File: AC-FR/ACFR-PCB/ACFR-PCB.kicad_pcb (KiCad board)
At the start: 4 copper layers, 46 x 26 mm, 65 parts, among them J1 USB4105-GF-A, J2 Micro_SD_Card_Det1, J3 JST-SM04B-SRSS, J4 JST-PH, Q1 DMP2045U-7, Q2 DMP2045U-7, SW1 PTS636 SK25F, SW2 PTS636 SK25F, U1 ESP32-S3R8, U2 BMP390, U3 W25Q128JVPIQ, U4 W25Q128JVPIQ, U5 LSM6DSO32, U6 H3LIS331DLTR, U7 AP2112K-3.3TRG1, U8 LIS3MDL, U9 AP2112K-3.3TRG1, Y1 ECS-400-8-36B-7KY

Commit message: Redo power
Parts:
- removed the C17 at (199.3, 115.3)
- removed C19, C21: 10uF, Capacitor_SMD:C_0603_1608Metric
- removed the C7 at (41.1, 155.3)
- removed H3: M2.5_2.7mm, MountingHole:MountingHole_2.7mm_M2.5_Pad_Via
- removed TP3: TestPoint, TestPoint:TestPoint_Pad_D1.5mm
- removed U9: AP2112K-3.3TRG1, Package_TO_SOT_SMD:SOT-23-5
- added C15: 1uF, Capacitor_SMD:C_0603_1608Metric, F.Cu at (162.6, 91.0)
- BZ1, D2, J2, J3, Q1, R10, R11, R12, R13, R4, R8, R9, U4: moved to B.Cu
- C11: renamed from C12; moved to B.Cu
- H1, H2: footprint MountingHole:MountingHole_2.7mm_M2.5_Pad_Via -> besser_footprints:M2.5_2.7mm_hole
- U7: value AP2112K-3.3TRG1 -> NCP187AMT330TAG; footprint Package_TO_SOT_SMD:SOT-23-5 -> besser_footprints:6-WDFN_2x2mm_EP
- moved J3 138.6 mm to (169.7, 98.3), turned to -90 degrees
- moved C6 125.4 mm to (164.4, 130.1)
- moved C7 119.4 mm to (134.7, 89.1), turned to 180 degrees
- moved U2 118.6 mm to (134.7, 91.1), turned to 90 degrees
- moved C5 117.2 mm to (157.8, 139.8), turned to -90 degrees
- moved C4 113.2 mm to (153.2, 132.2), turned to 180 degrees
- moved C3 113.0 mm to (153.2, 130.8), turned to 180 degrees
- moved R11 109.1 mm to (153.3, 102.3)
- moved R12 109.1 mm to (153.3, 105.3)
- moved R13 109.1 mm to (153.3, 108.3)
- moved C12 106.4 mm to (129.5, 97.2)
- moved U5 106.4 mm to (129.5, 94.8)
- moved C18 104.8 mm to (132.6, 94.8)
- moved U8 104.8 mm to (134.7, 94.8)
- moved C17 104.8 mm to (135.2, 97.0)
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- renumbered C11 to C10, C13 to C12, C14 to C13, C15 to C14, C18 to C17, C20 to C18, C8 to C7, C9 to C8, C10 to C9
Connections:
- C1 pad 1: +3V3_2 -> +3V3
- C11 pad 1: +3V3_2 -> +3V3
- C12 pad 1: +3V3_2 -> +3V3
- C13 pad 1: +3V3_2 -> +3V3
- C16 pad 2: VHIGH -> +3V3
- C17 pad 1: +3V3_2 -> +3V3
- C3 pad 1: +3V3_MCU -> +3V3
- C4 pad 1: +3V3_MCU -> +3V3
- C5 pad 1: +3V3_MCU -> +3V3
- C6 pad 1: +3V3_MCU -> +3V3
- C7 pad 2: +3V3_2 -> +3V3
- D1 pad 4: +3V3_2 -> +3V3
- J2 pad 11: GND -> (no net)
- J2 pad 12: GND -> (no net)
- J2 pad 4: +3V3_2 -> +3V3
- J2 pad 9: (no net) -> unconnected-(J2-DET-Pad9)
- R10 pad 1: +3V3_2 -> +3V3
- R11 pad 1: +3V3_2 -> +3V3
- R12 pad 1: +3V3_2 -> +3V3
- R13 pad 1: +3V3_2 -> +3V3
- R3 pad 2: +3V3_MCU -> +3V3
- R6 pad 2: +3V3_2 -> +3V3
- R7 pad 2: +3V3_2 -> +3V3
- R8 pad 1: +3V3_2 -> +3V3
- R9 pad 1: +3V3_2 -> +3V3
- TP1 pad 1: /IO11 -> /IO10
- TP2 pad 1: /IO12 -> /IO11
- U1 pad 10: /MISO -> /MOSI
- U1 pad 11: /SCK -> /MISO
- U1 pad 12: /FSH_CS -> /SCK
- U1 pad 14: /VBAT_SENSE -> /FSH_CS
- U1 pad 15: /NEOPIXEL -> /IO10
- U1 pad 17: /IO12 -> unconnected-(U1-GPIO12-Pad17)
- U1 pad 18: /IO13 -> unconnected-(U1-GPIO13-Pad18)
- U1 pad 19: /IMU_INT -> unconnected-(U1-GPIO14-Pad19)
- U1 pad 2: +3V3_MCU -> +3V3
- U1 pad 20: +3V3_MCU -> +3V3
- U1 pad 3: +3V3_MCU -> +3V3
- U1 pad 46: +3V3_MCU -> +3V3
- U1 pad 55: +3V3_MCU -> +3V3
- U1 pad 56: +3V3_MCU -> +3V3
- U1 pad 6: unconnected-(U1-GPIO1-Pad6) -> /NEOPIXEL
- U1 pad 9: /MOSI -> /VBAT_SENSE
- U2 pad 1: +3V3_2 -> +3V3
- U2 pad 10: +3V3_2 -> +3V3
- U2 pad 5: +3V3_2 -> +3V3
- U2 pad 6: +3V3_2 -> +3V3
- U4 pad 8: +3V3_2 -> +3V3
- U5 pad 12: +3V3_2 -> +3V3
- U5 pad 4: /IMU_INT -> unconnected-(U5-INT1-Pad4)
- U5 pad 5: +3V3_2 -> +3V3
- U5 pad 8: +3V3_2 -> +3V3
- U6 pad 1: +3V3_2 -> +3V3
- U6 pad 14: +3V3_2 -> +3V3
- U6 pad 15: +3V3_2 -> +3V3
- U6 pad 8: +3V3_2 -> +3V3
- U7 pad 2: GND -> VHIGH
- U7 pad 3: VHIGH -> GND
- U7 pad 5: +3V3_MCU -> +3V3
- U8 pad 10: +3V3_2 -> +3V3
- U8 pad 5: +3V3_2 -> +3V3
- U8 pad 6: +3V3_2 -> +3V3
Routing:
- net /SPICS0: track 0.00 -> 13.1 mm, vias 0 -> 2
- net /SPIQ: track 0.00 -> 11.2 mm, vias 0 -> 2
- net /SPIWP: track 0.00 -> 8.43 mm, vias 0 -> 2
- net /VDD_SPI: track 0.00 -> 6.91 mm
- net /SPIHD: track 0.00 -> 2.72 mm
- net /SPID: track 0.00 -> 2.61 mm
- net /SPICLK: track 0.00 -> 2.41 mm
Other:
- board text added: "3.7/4.2v 1S LiPo"

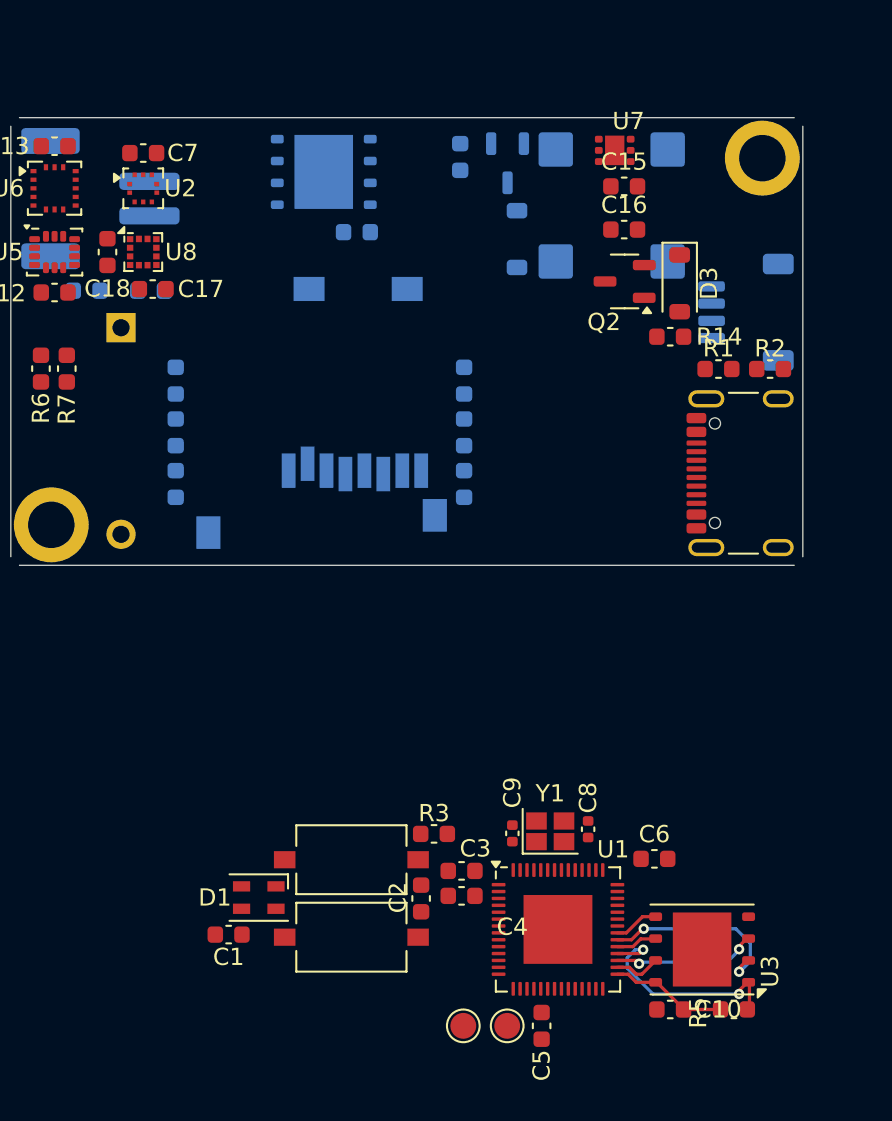
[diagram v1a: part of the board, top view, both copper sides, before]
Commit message: why do the colors not not stay after a crash this was supposed to be fixed in fucking 8.0.2
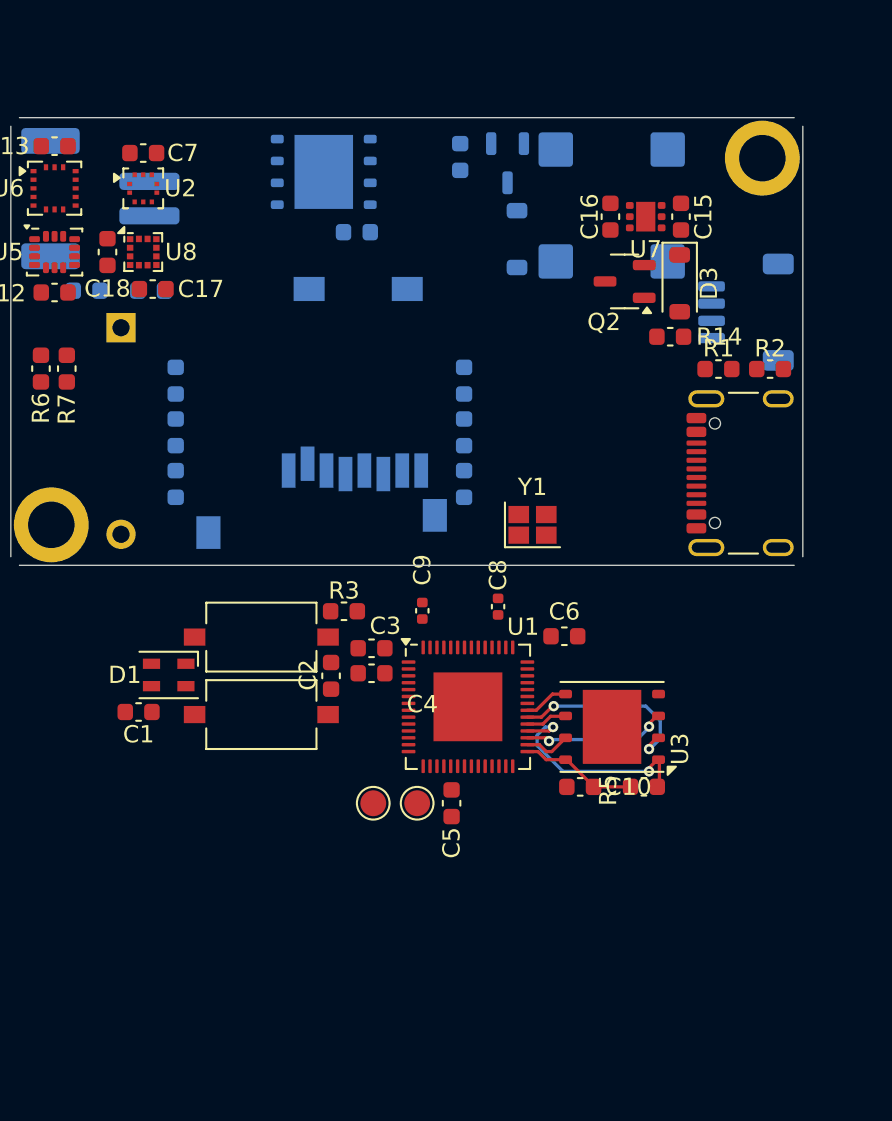
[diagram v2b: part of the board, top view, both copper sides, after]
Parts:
- moved Y1 17.8 mm to (157.3, 110.7)
- moved C10 13.9 mm to (160.1, 125.9)
- moved C3 13.9 mm to (147.9, 117.8)
- moved C5 13.9 mm to (152.6, 126.8)
- moved D1 13.9 mm to (136.2, 119.4)
- moved TP2 13.9 mm to (150.6, 126.8)
- moved C6 13.9 mm to (159.2, 117.1)
- moved C8 13.9 mm to (155.3, 115.4)
- moved TP1 13.9 mm to (148.1, 126.8)
- moved U1 13.9 mm to (153.6, 121.2)
- moved C1 13.9 mm to (134.4, 121.5)
- moved C2 13.9 mm to (145.6, 119.4)
- moved C4 13.9 mm to (147.9, 119.3)
- moved R3 13.9 mm to (146.3, 115.7)
- moved U3 13.9 mm to (161.9, 122.4)
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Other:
- board text added: "+"
- board text added: "-"
- board text added: "1S LiPo"
- board text added: "FD Flash"
- board text added: "R1 11-2024"
- board text removed: "3.7/4.2v 1S LiPo"

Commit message: Finalize part placement
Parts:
- C15, C16, D3, Q2, R14, U7: moved to B.Cu
- moved C15 38.0 mm to (128.6, 99.9)
- moved D3 37.5 mm to (129.0, 103.8)
- moved R14 36.7 mm to (129.3, 106.9), turned to 0 degrees
- moved C18 36.0 mm to (168.7, 94.2)
- moved C17 36.0 mm to (171.2, 96.2)
- moved C12 36.0 mm to (165.5, 96.5)
- moved U5 36.0 mm to (165.5, 94.2)
- moved U6 36.0 mm to (165.5, 90.5)
- moved U8 36.0 mm to (170.7, 94.2)
- moved C13 36.0 mm to (165.5, 88.2)
- moved U7 34.0 mm to (130.7, 99.9), turned to 0 degrees
- moved R6 32.8 mm to (160.7, 94.2)
- moved R7 32.8 mm to (162.2, 94.2)
- moved Q2 31.3 mm to (132.2, 103.7), turned to 0 degrees
- moved C16 30.0 mm to (132.7, 99.9)
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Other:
- outline, holes or cut-outs redrawn

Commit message: Start on routing (kill the project, its horrible)
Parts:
- removed J3: JST-SM04B-SRSS, besser_footprints:JST_SH_SM04B-SRSS-TB_1x04-1MP_P1.00mm_Horizontal
- added R8: 47k, Capacitor_SMD:C_0603_1608Metric, B.Cu at (161.3, 110.2)
- moved C3 30.8 mm to (146.8, 130.3)
- moved C5 30.8 mm to (151.7, 139.3)
- moved R3 30.8 mm to (146.8, 128.8)
- moved U3 30.8 mm to (160.8, 134.9)
- moved TP1 30.8 mm to (146.9, 139.3)
- moved TP2 30.8 mm to (149.5, 139.3)
- moved C4 30.8 mm to (146.8, 131.8)
- moved C6 30.8 mm to (155.8, 128.8)
- moved C9 30.8 mm to (148.8, 127.8)
- moved R5 30.8 mm to (162.6, 138.3)
- moved C1 30.8 mm to (138.8, 130.8)
- moved C10 30.8 mm to (158.9, 138.3)
- moved C2 30.8 mm to (144.6, 131.0)
- moved C8 30.8 mm to (153.2, 127.6)
- moved D1 30.8 mm to (141.2, 130.8)
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- renumbered C17 to C16, C18 to C17, C16 to C18, R9 to R10, R10 to R11, R11 to R12, R12 to R13, R13 to R14, R14 to R17, R8 to R9, U8 to U7, U7 to U8
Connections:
- net VHIGH renamed /VHIGH
- U1 pad 11: /MISO -> /SD_CS
- U1 pad 13: /SD_CS -> /MISO
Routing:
- net +3V3: track 0.00 -> 60.4 mm
- net VBUS: track 0.00 -> 59.9 mm, vias 0 -> 1
- net /MOSI: track 0.00 -> 33.8 mm, vias 0 -> 2
- net VBAT: track 0.00 -> 23.9 mm
- net /VHIGH: track 0.00 -> 23.8 mm, vias 0 -> 2
- net /SCL: track 0.00 -> 21.5 mm, vias 0 -> 4
- net /SDA: track 0.00 -> 20.1 mm, vias 0 -> 3
- net /SCK: track 0.00 -> 14.1 mm
- net /MISO: track 0.00 -> 12.6 mm
- net /SD_CS: track 0.00 -> 9.42 mm
- net Net-(J2-DAT2): track 0.00 -> 6.56 mm
- net GND: track 0.00 -> 5.86 mm, vias 0 -> 2
- net Net-(BZ1--): track 0.00 -> 5.53 mm
- net /D-: track 0.00 -> 4.27 mm
- net /D+: track 0.00 -> 3.50 mm
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- added copper zone on B.Cu, net GND
- added copper zone on F.Cu, net GND
- added copper zone on In1.Cu, net GND
- added copper zone on In2.Cu, net GND

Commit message: Finally make progress on layout and routing
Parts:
- BZ1, C11, D2, Q1, R4, R8, U4: moved to F.Cu
- TP1, TP2: footprint TestPoint:TestPoint_Pad_D1.5mm -> TestPoint:TestPoint_Pad_1.0x1.0mm
- moved U2 56.1 mm to (205.6, 55.1)
- moved C7 56.1 mm to (205.6, 53.2)
- moved R7 55.3 mm to (197.1, 54.9), turned to 90 degrees
- moved R6 54.1 mm to (195.5, 56.5), turned to 90 degrees
- moved C12 49.7 mm to (200.4, 61.1)
- moved C13 49.7 mm to (200.4, 52.8)
- moved C16 49.7 mm to (206.1, 60.9)
- moved C17 49.7 mm to (203.6, 58.9)
- moved U5 49.7 mm to (200.4, 58.9)
- moved U6 49.7 mm to (200.4, 55.2)
- moved U7 49.7 mm to (205.6, 58.9)
- moved R16 47.4 mm to (135.1, 144.3), turned to 90 degrees
- moved R5 45.3 mm to (144.7, 96.7), turned to 0 degrees
- moved R15 44.3 mm to (135.1, 141.3), turned to 90 degrees
- moved C10 43.0 mm to (148.4, 96.7), turned to 0 degrees
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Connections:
- SW1 pad 1: /BOOT -> GND
- SW1 pad 2: GND -> /BOOT
- U1 pad 10: /MOSI -> /SD_CS
- U1 pad 11: /SD_CS -> /MISO
- U1 pad 12: /SCK -> /FSH_CS
- U1 pad 13: /MISO -> /MOSI
- U1 pad 14: /FSH_CS -> /SCK
- U1 pad 18: unconnected-(U1-GPIO13-Pad18) -> /VBAT_SENSE
- U1 pad 43: unconnected-(U1-GPIO38-Pad43) -> /NEOPIXEL
- U1 pad 51: unconnected-(U1-GPIO45-Pad51) -> /BUZZ
- U1 pad 6: /NEOPIXEL -> unconnected-(U1-GPIO1-Pad6)
- U1 pad 9: /VBAT_SENSE -> unconnected-(U1-GPIO4-Pad9)
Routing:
- net VBUS: track 59.9 -> 0.00 mm, vias 1 -> 0
- net VBAT: track 23.9 -> 0.00 mm
- net /VHIGH: track 23.8 -> 0.00 mm, vias 2 -> 0
- net /D-: track 4.27 -> 27.7 mm
- net /D+: track 3.50 -> 26.5 mm
- net /SCL: track 21.5 -> 0.00 mm, vias 4 -> 0
- net /MISO: track 12.6 -> 33.7 mm, vias 0 -> 1
- net /SDA: track 20.1 -> 0.00 mm, vias 3 -> 0
- net /SD_CS: track 9.42 -> 28.8 mm, vias 0 -> 1
- net +3V3: track 60.4 -> 44.4 mm, vias 0 -> 2
- net /RESET: track 0.00 -> 11.7 mm
- net /SCK: track 14.1 -> 25.6 mm, vias 0 -> 1
- net /FSH_CS: track 0.00 -> 9.84 mm
- net /BUZZ: track 1.50 -> 8.99 mm
- net /BOOT: track 0.00 -> 6.36 mm
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- added copper zone on F.Cu, net +3V3
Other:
- board text added: "Rotate MCU parts moce JST connector over USB for more room for power parts"

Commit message: Work on routing
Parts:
- moved U2 69.2 mm to (146.3, 90.9)
- moved C7 69.0 mm to (146.3, 88.6)
- moved C13 61.4 mm to (150.4, 88.6)
- moved U6 61.4 mm to (150.4, 90.9)
- moved U7 60.1 mm to (154.8, 90.9), turned to 180 degrees
- moved C16 58.8 mm to (154.2, 88.6), turned to 180 degrees
- moved R7 57.7 mm to (154.6, 93.9), turned to 0 degrees
- moved C17 56.6 mm to (156.8, 90.8), turned to -90 degrees
- moved R6 55.9 mm to (155.3, 95.4), turned to 0 degrees
- moved C14 53.5 mm to (139.8, 90.3), turned to -90 degrees
- moved U5 51.3 mm to (160.3, 90.9), turned to 180 degrees
- moved R16 49.5 mm to (136.9, 94.8), turned to 0 degrees
- moved C12 48.6 mm to (160.3, 88.6), turned to 180 degrees
- moved R17 48.0 mm to (130.6, 93.8), turned to 90 degrees
- moved R15 48.0 mm to (136.9, 93.3), turned to 180 degrees
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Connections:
- TP1 pad 1: /IO10 -> /IO4
- U1 pad 15: /IO10 -> /IO11
- U1 pad 16: /IO11 -> unconnected-(U1-GPIO11-Pad16)
- U1 pad 9: unconnected-(U1-GPIO4-Pad9) -> /IO4
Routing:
- net +3V3: track 44.4 -> 114.2 mm, vias 2 -> 3
- net GND: track 6.97 -> 31.6 mm, vias 6 -> 36
- net /VBAT_SENSE: track 0.00 -> 22.7 mm, vias 0 -> 1
- net VBUS: track 0.00 -> 16.9 mm, vias 0 -> 1
- net /VHIGH: track 0.00 -> 16.8 mm
- net VBAT: track 0.00 -> 16.3 mm
- net /SCL: track 0.00 -> 4.76 mm
- net /IO11: track 0.00 -> 3.23 mm
- net /SDA: track 0.00 -> 3.09 mm
- net /IO4: track 0.00 -> 2.57 mm
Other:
- board text removed: "Ensure board is centered on 0,0 Add BC image to silkscreen Set up board constraints, stackup, settings, netclasses before starting"
- board text removed: "Rotate MCU parts moce JST connector over USB for more room for power parts"

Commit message: Continue work on routing
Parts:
- added J3: JST-SM04B-SRSS, besser_footprints:JST_SH_SM04B-SRSS-TB_1x04-1MP_P1.00mm_Horizontal, F.Cu at (130.3, 90.9)
- added REF**: ublox_ZOE_M8, RF_GPS:ublox_ZOE_M8, B.Cu at (140.1, 109.6)
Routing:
- net /VHIGH: track 16.8 -> 46.1 mm, vias 0 -> 1
- net +3V3: track 114.2 -> 124.2 mm, vias 3 -> 4
- net GND: track 31.6 -> 37.2 mm, vias 36 -> 32
- net /SDA: track 3.09 -> 4.77 mm
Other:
- board text added: "CARFIO"
- board text added: "Make ChungRF have hte same mounting hole positions for easier avioncs stacking Dont forget stitching vias"

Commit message: ACFR R1
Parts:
- removed REF**: ublox_ZOE_M8, RF_GPS:ublox_ZOE_M8
- Q1: value DMP2045U-7 -> NXV55UNR
- moved H2 33.7 mm to (138.9, 78.2), turned to -90 degrees
- moved D3 31.8 mm to (156.2, 77.3), turned to 180 degrees
- moved H1 31.5 mm to (159.9, 119.2), turned to -90 degrees
- moved C15 30.6 mm to (159.1, 79.2), turned to 180 degrees
- moved J3 30.6 mm to (158.5, 79.0), turned to 180 degrees
- moved J1 29.8 mm to (146.7, 78.3), turned to 180 degrees
- moved R17 29.0 mm to (155.6, 79.2), turned to 0 degrees
- moved U8 28.1 mm to (159.1, 81.2), turned to -90 degrees
- moved SW2 27.5 mm to (139.8, 115.4), turned to 90 degrees
- moved U4 26.4 mm to (149.8, 117.7), turned to 0 degrees
- moved R9 26.3 mm to (141.2, 115.2), turned to -90 degrees
- moved J4 25.9 mm to (149.2, 80.8), turned to 0 degrees
- moved C18 25.6 mm to (159.1, 83.2), turned to 180 degrees
- moved R14 25.3 mm to (158.1, 115.2), turned to -90 degrees
- moved Q2 25.2 mm to (155.6, 82.0), turned to -90 degrees
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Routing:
- net +3V3: track 124.2 -> 169.1 mm
- net /SDA: track 4.77 -> 39.6 mm, vias 0 -> 2
- net /SCL: track 4.76 -> 38.6 mm, vias 0 -> 5
- net GND: track 37.2 -> 59.3 mm, vias 32 -> 71
- net Net-(BZ1--): track 8.20 -> 5.68 mm
- net Net-(U7-C1): track 0.00 -> 1.30 mm
- net /BUZZ: track 9.28 -> 10.4 mm
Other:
- board size 46 x 26 mm -> 26 x 46 mm
- board text added: "ACFR"
- board text added: "B"
- board text added: "MicroSD"
- board text added: "R"
- board text removed: "Make ChungRF have hte same mounting hole positions for easier avioncs stacking Dont forget stitching vias"
